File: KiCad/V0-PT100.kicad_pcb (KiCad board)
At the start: 2 copper layers, 21 parts, among them J1 T1, J2 T2, J3 SPI1, J4 E0-Stop, U1 MAX31865ATP+, U2 MIC5225-3.3YM5-TR

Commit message: Swap out some component
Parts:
- J4: value E0-Stop -> Servos
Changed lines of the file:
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@@
     (38 B.Mask user)
     (39 F.Mask user)
-    (40 Dwgs.User user)
+    (40 Dwgs.User user hide)
     (41 Cmts.User user)
     (42 Eco1.User user)
@@
     (pad_to_mask_clearance 0.05)
     (aux_axis_origin 0 0)
-    (visible_elements FFFFFF7F)
+    (visible_elements FFFFF77F)
     (pcbplotparams
       (layerselection 0x010fc_ffffffff)
@@
       (effects (font (size 1 1) (thickness 0.15)))
     )
-    (fp_text value E0-Stop (at 4.385 4.81) (layer F.Fab)
+    (fp_text value Servos (at 4.385 4.81) (layer F.Fab)
       (effects (font (size 1 1) (thickness 0.15)))
     )
@@
       (effects (font (size 1 1) (thickness 0.15)))
     )
-    (fp_text value MAX31865ATP+ (at 0 0) (layer F.SilkS)
-      (effects (font (size 1 1) (thickness 0.15)))
-    )
+    (fp_text value MAX31865ATP+ (at 0 -5.08) (layer F.SilkS)
+      (effects (font (size 1 1) (thickness 0.15)))
+    )

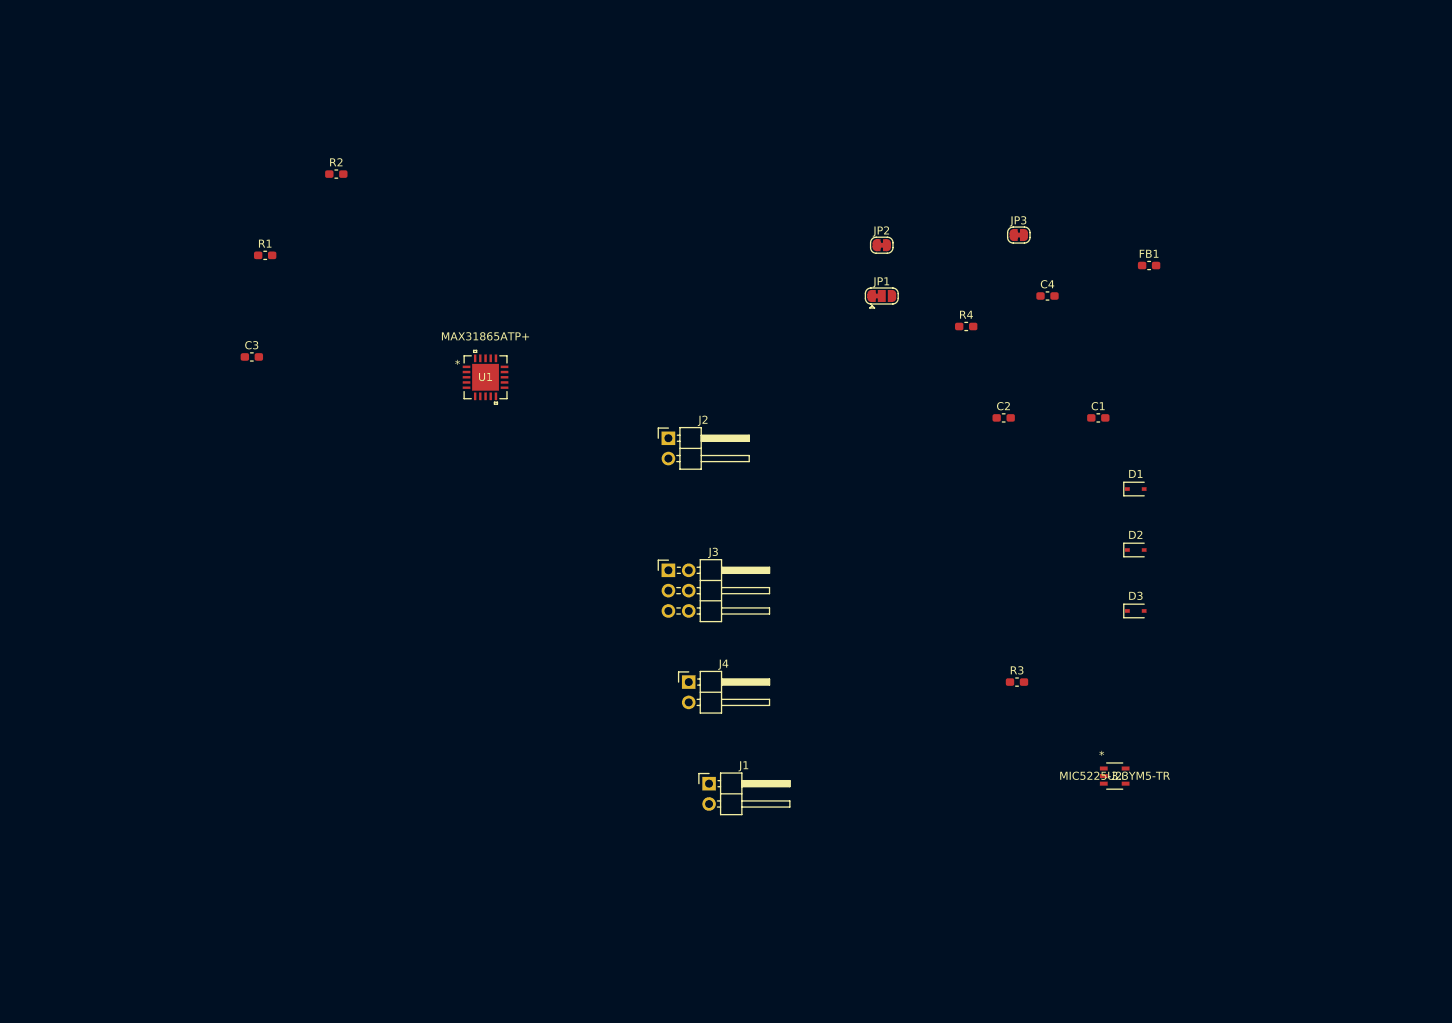
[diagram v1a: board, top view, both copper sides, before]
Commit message: Update PCB parts
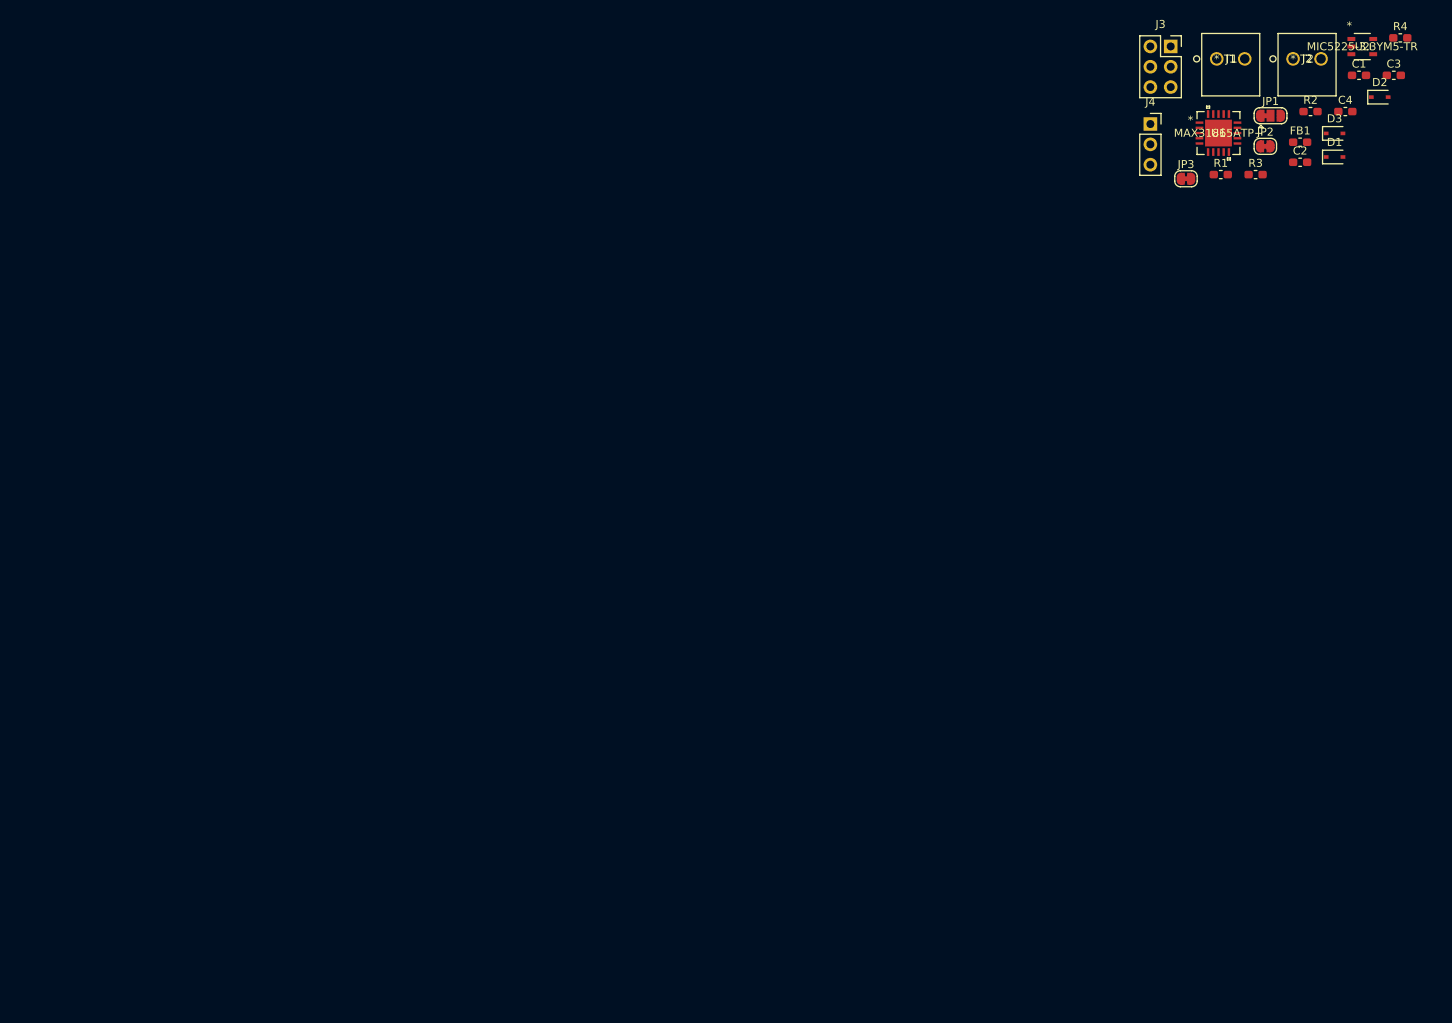
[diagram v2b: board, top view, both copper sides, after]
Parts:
- J1, J2: footprint Connector_PinHeader_2.54mm:PinHeader_1x02_P2.54mm_Horizontal -> V0PT100:1984617
- J3: footprint Connector_PinHeader_2.54mm:PinHeader_2x03_P2.54mm_Horizontal -> Connector_PinSocket_2.54mm:PinSocket_2x03_P2.54mm_Vertical
- J4: footprint Connector_PinHeader_2.54mm:PinHeader_1x02_P2.54mm_Horizontal -> Connector_PinSocket_2.54mm:PinSocket_1x03_P2.54mm_Vertical
- moved C3 147.0 mm to (276.1, 24.5)
- moved R2 122.0 mm to (265.7, 29.0)
- moved R1 119.9 mm to (254.5, 36.9)
- moved J1 110.6 mm to (254.0, 22.4)
- moved U1 96.6 mm to (254.2, 31.7)
- moved U2 96.3 mm to (272.2, 20.9)
- moved J2 91.4 mm to (263.5, 22.4)
- moved J3 90.7 mm to (248.2, 20.9)
- moved J4 90.5 mm to (245.7, 30.6)
- moved R3 70.1 mm to (258.8, 36.9)
- moved R4 65.2 mm to (276.9, 19.8)
- moved D3 64.7 mm to (268.7, 31.7)
- moved D2 64.3 mm to (274.3, 27.2)
- moved C1 53.8 mm to (271.7, 24.5)
- moved JP1 53.6 mm to (260.7, 29.5)
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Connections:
- J4 pad 2: /CS -> Net-(J4-Pad2)

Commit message: Inital PCB layout complete
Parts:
- J4: value Servos -> Output; footprint Connector_PinSocket_2.54mm:PinSocket_1x03_P2.54mm_Vertical -> Connector_PinHeader_2.54mm:PinHeader_1x01_P2.54mm_Horizontal
- moved R4 191.7 mm to (114.8, 122.2), turned to 180 degrees
- moved J2 185.9 mm to (115.3, 134.6)
- moved J1 183.9 mm to (108.2, 134.6)
- moved C1 182.4 mm to (114.8, 117.3)
- moved D2 181.7 mm to (120.4, 123.7), turned to 180 degrees
- moved JP1 181.1 mm to (106.9, 125.2), turned to 180 degrees
- moved C3 180.8 mm to (116.2, 108.7)
- moved U2 180.5 mm to (116.2, 111.8), turned to 270 degrees
- moved C4 179.5 mm to (114.8, 119.0)
- moved R2 178.1 mm to (114.8, 123.6), turned to 180 degrees
- moved JP2 177.9 mm to (110.0, 128.9), turned to 180 degrees
- moved FB1 175.4 mm to (109.6, 115.4), turned to 180 degrees
- moved R3 174.2 mm to (105.4, 119.4), turned to 90 degrees
- moved D1 174.0 mm to (120.4, 125.7), turned to 180 degrees
- moved D3 173.4 mm to (120.4, 121.6), turned to 180 degrees
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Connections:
- net Net-(C2-Pad1) renamed /VDD
- net Net-(R3-Pad1) renamed /ISENSOR
- net Net-(R3-Pad2) renamed /BIAS
- J1 pad 1: /M-RTDIN+ -> /FORCE+
- J1 pad 2: /FORCE+ -> /M-RTDIN+
- J2 pad 1: /FORCE- -> /M-RTDIN-
- J2 pad 2: /M-RTDIN- -> /FORCE-
- J4 pad 1: GND -> /CS
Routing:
- net GND: track 0.00 -> 52.7 mm, vias 0 -> 3
- net /SDI: track 0.00 -> 33.4 mm, vias 0 -> 1
- net +3V3: track 0.00 -> 28.1 mm, vias 0 -> 4
- net /SCK: track 0.00 -> 25.4 mm, vias 0 -> 1
- net +5V: track 0.00 -> 19.6 mm, vias 0 -> 1
- net /FORCE-: track 0.00 -> 18.7 mm
- net /M-RTDIN-: track 0.00 -> 18.1 mm
- net /FORCE+: track 0.00 -> 17.6 mm
- net /SDO: track 0.00 -> 16.0 mm, vias 0 -> 1
- net /M-RTDIN+: track 0.00 -> 13.3 mm
- net /M-SDI: track 0.00 -> 12.7 mm, vias 0 -> 2
- net /M-SCK: track 0.00 -> 9.35 mm, vias 0 -> 3
- net /VDD: track 0.00 -> 9.07 mm
- net /M-CS: track 0.00 -> 8.94 mm, vias 0 -> 2
- net /M-FORCE2: track 0.00 -> 4.10 mm
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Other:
- board outline added: 19 x 33 mm

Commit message: Add files via upload
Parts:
- moved J1 0.83 mm to (107.8, 133.9)
- moved J2 0.74 mm to (115.3, 133.9)
- moved JP3 0.14 mm to (117.3, 128.9)
- moved D2 0.05 mm to (120.4, 123.6)
- moved R2 0.05 mm to (114.8, 123.7)
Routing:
- net GND: track 52.7 -> 19.3 mm
- net /SDI: track 33.4 -> 35.1 mm
- net /SCK: track 25.4 -> 27.1 mm
- net /SDO: track 16.0 -> 14.4 mm
- net +3V3: track 28.1 -> 29.6 mm, vias 4 -> 3
- net /M-FORCE2: track 4.10 -> 3.44 mm
- net +5V: track 19.6 -> 20.3 mm, vias 1 -> 0
- net /M-CS: track 8.94 -> 9.56 mm, vias 2 -> 0
- net /M-SCK: track 9.35 -> 9.80 mm, vias 3 -> 2
- net /M-SDI: track 12.7 -> 12.5 mm, vias 2 -> 0
- added copper zone on B.Cu, net GND
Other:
- board size 19 x 33 mm -> 19 x 30.8 mm
